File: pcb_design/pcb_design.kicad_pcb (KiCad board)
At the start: 2 copper layers, 6 parts, among them U1 ATmega2560-16AU

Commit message: Make PCB design
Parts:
- added C3: 100nF, Capacitor_SMD:C_0201_0603Metric, F.Cu at (137.2, 76.2)
- added C4: 100nF, Capacitor_SMD:C_0201_0603Metric, F.Cu at (137.2, 74.9)
- added C5: 100nF, Capacitor_SMD:C_0201_0603Metric, F.Cu at (137.2, 73.7)
- added D1: LED, LED_SMD:LED_0201_0603Metric, F.Cu at (132.1, 54.6)
- added D2: LED_PWR, LED_SMD:LED_0201_0603Metric, F.Cu at (99.1, 105.4)
- added J1: PWR_IN, Connector_PinHeader_2.54mm:PinHeader_1x02_P2.54mm_Vertical, F.Cu at (101.6, 102.9)
- added J10: PD, Connector_PinHeader_2.54mm:PinHeader_1x08_P2.54mm_Vertical, F.Cu at (171.4, 104.1)
- added J11: PE, Connector_PinHeader_2.54mm:PinHeader_1x08_P2.54mm_Vertical, F.Cu at (110.5, 43.2)
- added J12: PF, Connector_PinHeader_2.54mm:PinHeader_1x08_P2.54mm_Vertical, F.Cu at (110.5, 39.4)
- added J13: ICSP, Connector_PinHeader_2.54mm:PinHeader_2x03_P2.54mm_Vertical, F.Cu at (100.3, 88.9)
- added J14: PWR_OUT, Connector_PinHeader_2.54mm:PinHeader_1x02_P2.54mm_Vertical, F.Cu at (99.1, 99.1)
- added J2: ESP8266_CONN, Connector_PinHeader_2.54mm:PinHeader_2x04_P2.54mm_Vertical, F.Cu at (99.1, 62.2)
- added J3: PL, Connector_PinHeader_2.54mm:PinHeader_1x08_P2.54mm_Vertical, F.Cu at (149.9, 104.1)
- added J4: PK, Connector_PinHeader_2.54mm:PinHeader_1x08_P2.54mm_Vertical, F.Cu at (132.1, 39.4)
- added J5: PJ, Connector_PinHeader_2.54mm:PinHeader_1x08_P2.54mm_Vertical, F.Cu at (171.4, 61.0)
- added J6: PH, Connector_PinHeader_2.54mm:PinHeader_1x05_P2.54mm_Vertical, F.Cu at (110.5, 64.8)
- added J7: PA, Connector_PinHeader_2.54mm:PinHeader_1x08_P2.54mm_Vertical, F.Cu at (153.7, 39.4)
- added J8: PB, Connector_PinHeader_2.54mm:PinHeader_1x08_P2.54mm_Vertical, F.Cu at (110.5, 81.3)
- added J9: PC, Connector_PinHeader_2.54mm:PinHeader_1x08_P2.54mm_Vertical, F.Cu at (171.4, 82.5)
- added R3: 10K, Resistor_SMD:R_0201_0603Metric, F.Cu at (100.3, 59.7)
- added R4: 20K, Resistor_SMD:R_0201_0603Metric, F.Cu at (97.8, 59.7)
- added R7: 1K, Resistor_SMD:R_0201_0603Metric, F.Cu at (130.8, 54.6)
- added R8: 10K, Resistor_SMD:R_0201_0603Metric, F.Cu at (102.9, 86.4)
- added R9: 1K, Resistor_SMD:R_0201_0603Metric, F.Cu at (100.3, 105.4)
- added SW1: SW_Push, Button_Switch_SMD:SW_SPST_B3U-1000P, F.Cu at (99.1, 83.8)
- added U2: LD1117S33TR_SOT223, Package_TO_SOT_SMD:SOT-223-3_TabPin2, F.Cu at (101.6, 76.2)
- C1, C2: footprint Capacitor_SMD:C_0603_1608Metric -> Capacitor_SMD:C_0201_0603Metric
- R1, R2: footprint Resistor_SMD:R_1806_4516Metric_Pad1.57x1.80mm_HandSolder -> Resistor_SMD:R_0201_0603Metric
- moved R1 52.8 mm to (139.7, 88.9), turned to 180 degrees
- moved C2 39.9 mm to (138.4, 86.4), turned to 90 degrees
- moved Clk1 36.0 mm to (142.2, 82.5), turned to 180 degrees
- moved C1 35.3 mm to (141.0, 86.4), turned to 90 degrees
- moved R2 27.4 mm to (138.4, 77.5), turned to 270 degrees
- moved U1 12.8 mm to (141.0, 63.5)
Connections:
- net /GND renamed GND
- net Net-(U1-Pad51) renamed /PG0
- net Net-(U1-Pad52) renamed /PG1
- U1 pad 10: Net-(U1-Pad10) -> +5V
- U1 pad 100: Net-(U1-Pad100) -> +5V
- U1 pad 12: Net-(U1-Pad12) -> /ESP_TX
- U1 pad 13: Net-(U1-Pad13) -> /TX2
- U1 pad 2: Net-(U1-Pad2) -> /PRGM_RX
- U1 pad 20: Net-(U1-Pad20) -> /SCK
- U1 pad 21: Net-(U1-Pad21) -> /MOSI
- U1 pad 22: Net-(U1-Pad22) -> /MISO
- U1 pad 3: Net-(U1-Pad3) -> /PRGM_TX
- U1 pad 31: Net-(U1-Pad10) -> +5V
- U1 pad 61: Net-(U1-Pad10) -> +5V
- U1 pad 80: Net-(U1-Pad10) -> +5V
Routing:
- net +5V: track 0.00 -> 136.8 mm
- net /RST: track 0.00 -> 72.1 mm
- net /ESP_TX: track 0.00 -> 53.9 mm
- net /MISO: track 0.00 -> 48.2 mm
- net Net-(J10-Pad1): track 0.00 -> 44.6 mm
- net Net-(J5-Pad8): track 0.00 -> 43.3 mm
- net /SCK: track 0.00 -> 43.3 mm
- net Net-(J3-Pad8): track 0.00 -> 43.2 mm
- net Net-(J3-Pad7): track 0.00 -> 42.4 mm
- net Net-(J10-Pad2): track 0.00 -> 41.8 mm
- net Net-(J3-Pad6): track 0.00 -> 41.5 mm
- net Net-(J3-Pad5): track 0.00 -> 40.7 mm
- net /MOSI: track 0.00 -> 40.4 mm
- net Net-(J10-Pad3): track 0.00 -> 40.1 mm
- net Net-(J3-Pad4): track 0.00 -> 39.9 mm
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- added copper zone on B.Cu, net GND

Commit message: Almost done?
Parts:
- added JP1: IO0_JMP, Connector_PinHeader_2.54mm:PinHeader_1x02_P2.54mm_Vertical, F.Cu at (99.1, 45.7)
- added JP2: RST_JMP, Connector_PinHeader_2.54mm:PinHeader_1x02_P2.54mm_Vertical, F.Cu at (102.9, 45.7)
- added R5: 10k, Resistor_SMD:R_0201_0603Metric, F.Cu at (100.3, 52.1)
- added R6: 10k, Resistor_SMD:R_0201_0603Metric, F.Cu at (101.6, 52.1)
- D1: value LED -> FUN_LED_YEL
- D2: value LED_PWR -> LED_PWR_GRN
- moved R3 4.02 mm to (99.1, 55.9)
- moved J14 3.81 mm to (102.9, 99.1), turned to 270 degrees
- moved J2 3.81 mm to (99.1, 58.4)
- moved R4 3.81 mm to (97.8, 55.9)
- moved R8 1.59 mm to (101.3, 86.4), turned to 180 degrees
- moved J1 1.27 mm to (102.9, 102.9)
- moved R7 1.27 mm to (132.1, 54.6)
- moved D2 1.27 mm to (100.3, 105.4)
- moved J13 1.27 mm to (99.1, 88.9)
- moved R9 1.27 mm to (101.6, 105.4)
- moved U2 1.27 mm to (101.6, 74.9)
- moved D1 1.27 mm to (133.3, 54.6)
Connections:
- J14 pad 1: GND -> +5V
- J14 pad 2: +5V -> GND
- J2 pad 3: +3V3 -> /ESP_IO0
- J2 pad 4: +3V3 -> /ESP_RST
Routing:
- net GND: track 52.9 -> 186.2 mm, vias 9 -> 11
- net /ESP_IO0: track 0.00 -> 22.7 mm
- net /ESP_TX: track 53.9 -> 33.0 mm
- net /ESP_RST: track 0.00 -> 18.8 mm
- net Net-(J5-Pad8): track 43.3 -> 33.7 mm, vias 0 -> 2
- net /TX2: track 34.1 -> 42.2 mm, vias 0 -> 2
- net +3V3: track 24.3 -> 31.7 mm, vias 0 -> 2
- net +5V: track 136.8 -> 139.9 mm
- net /MISO: track 48.2 -> 50.1 mm
- net /MOSI: track 40.4 -> 41.6 mm
- net /SCK: track 43.3 -> 44.5 mm
- net /ESP_RX: track 4.44 -> 3.30 mm
- net /RST: track 72.1 -> 73.2 mm, vias 0 -> 1
- net Net-(D2-Pad2): track 0.00 -> 0.63 mm
- removed copper zone on B.Cu, net GND
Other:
- board text added: "3.3V"
- board text added: "5V"
- board text added: "A0"
- board text added: "B0"
- board text added: "C0"
- board text added: "D7"
- board text added: "E0"
- board text added: "ESP"
- board text added: "ESP JMP"
- board text added: "F0"
- board text added: "GND"
- board text added: "H2"
- board text added: "ICSP"
- board text added: "IO0"
- board text added: "J0"
- board text added: "K0"
- board text added: "L0"
- board text added: "RST"

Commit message: Add DS3231 RTC header
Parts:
- added J15: Conn_01x04, Connector_PinSocket_2.54mm:PinSocket_1x04_P2.54mm_Vertical, F.Cu at (134.6, 100.3)
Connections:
- net Net-(J10-Pad1) renamed /SCL
- net Net-(J10-Pad2) renamed /SDA
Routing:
- net /SDA: track 41.8 -> 82.3 mm
- net /SCL: track 44.6 -> 85.1 mm
- net +5V: track 139.9 -> 153.4 mm
- net GND: track 186.2 -> 193.6 mm

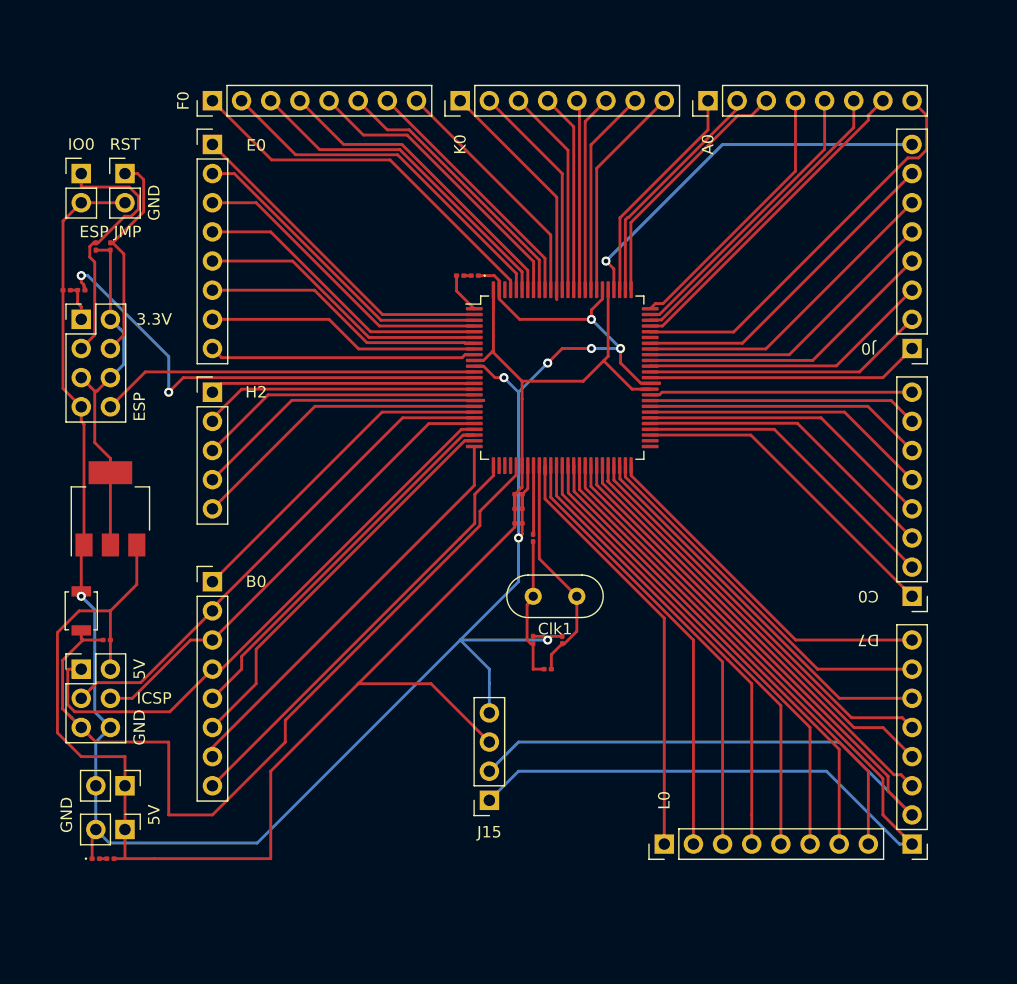
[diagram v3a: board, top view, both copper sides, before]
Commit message: Add lineout to PCB design
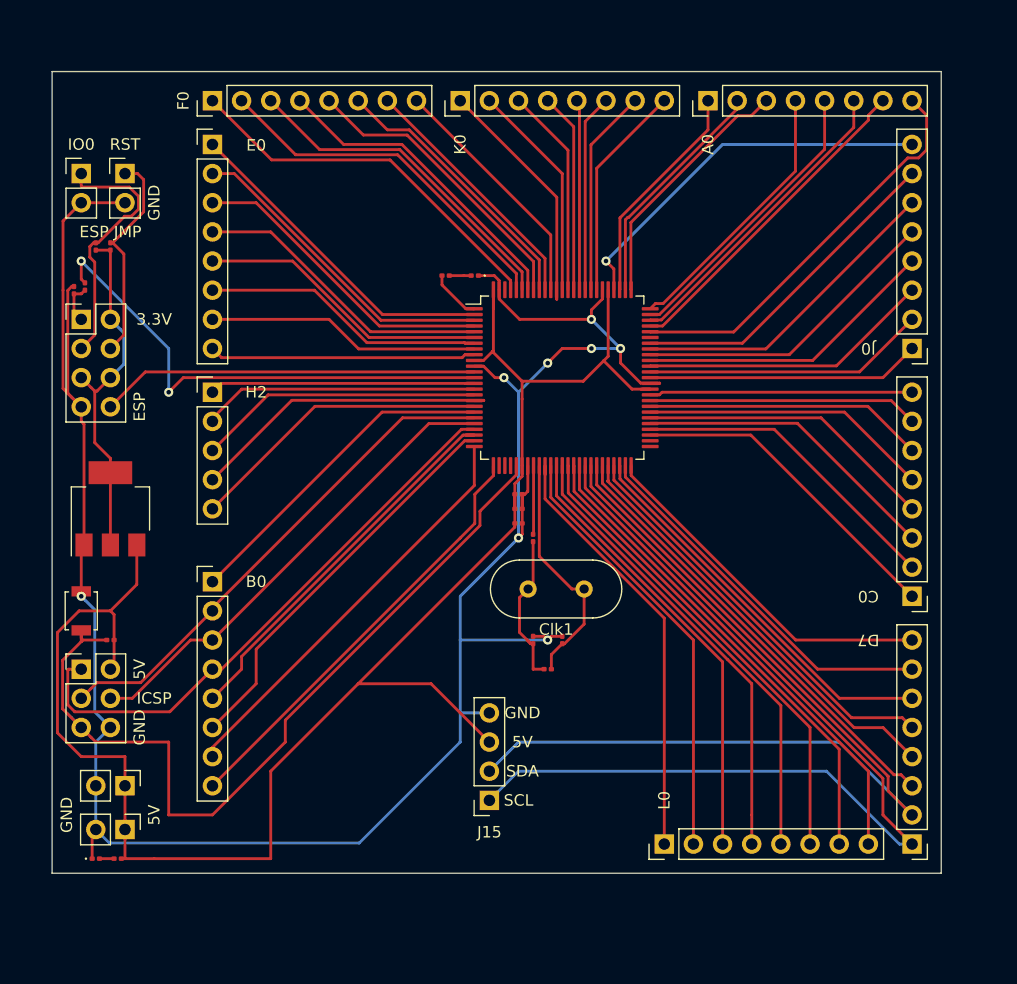
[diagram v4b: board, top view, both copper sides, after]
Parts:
- Clk1: footprint Crystal:Crystal_HC52-8mm_Vertical -> Crystal:Crystal_HC49-4H_Vertical
- moved R7 1.27 mm to (130.8, 54.6)
- moved Clk1 0.90 mm to (142.9, 81.9)
- moved R9 0.64 mm to (102.2, 105.4)
- moved R4 0.63 mm to (98.4, 55.9), turned to 90 degrees
- moved R3 0.45 mm to (99.4, 55.6), turned to 270 degrees
- moved R8 0.32 mm to (101.6, 86.4)
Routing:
- net GND: track 193.6 -> 205.4 mm
- net /TX2: track 42.2 -> 43.8 mm
- net Net-(C1-Pad1): track 20.1 -> 21.5 mm
- net Net-(D1-Pad2): track 0.63 -> 1.90 mm
- net /RST: track 73.2 -> 74.3 mm
- net Net-(C2-Pad1): track 12.6 -> 13.6 mm
- net Net-(R7-Pad2): track 3.86 -> 4.62 mm
- net Net-(D2-Pad2): track 0.63 -> 1.27 mm
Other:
- board outline added: 77.5 x 69.9 mm
- board text added: "SCL"
- board text added: "SDA"

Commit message: Add mounting holes
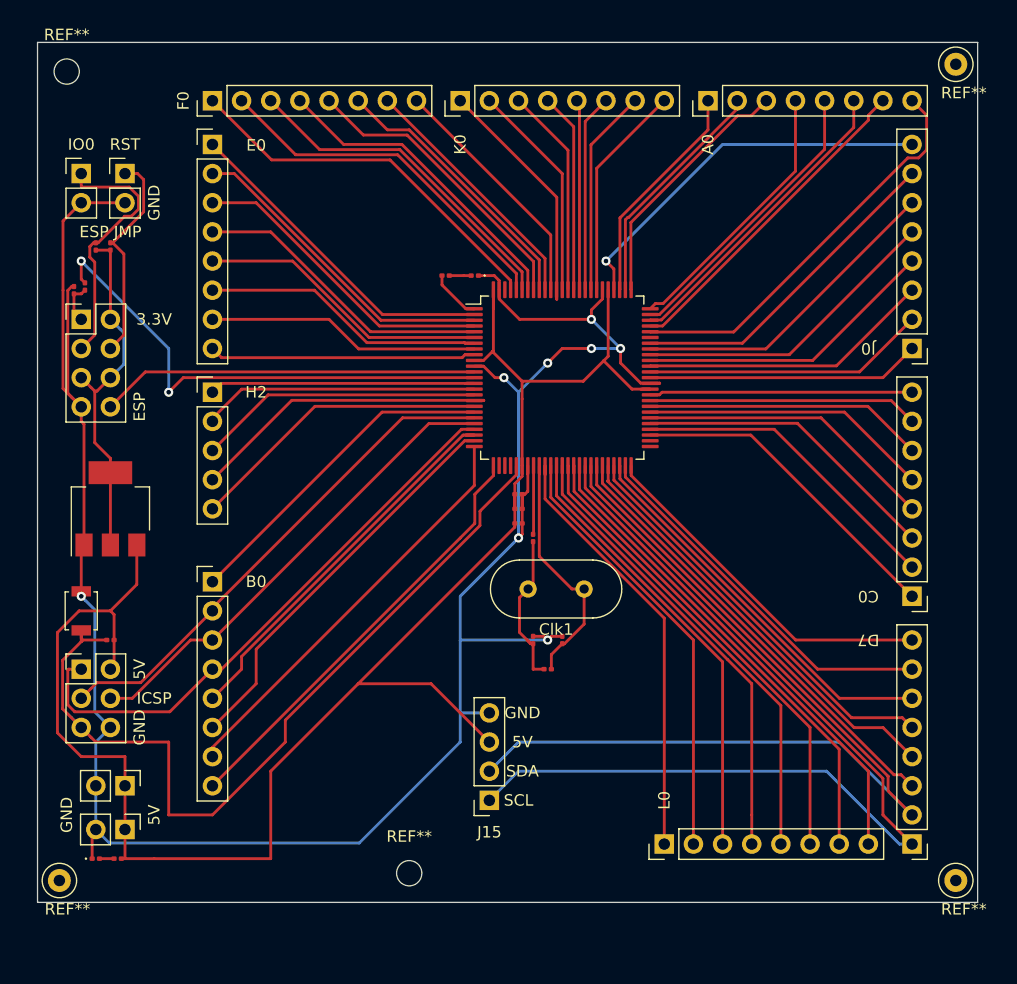
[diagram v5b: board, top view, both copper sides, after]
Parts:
- added REF**: TestPoint_Loop_D1.80mm_Drill1.0mm_Beaded, TestPoint:TestPoint_Loop_D1.80mm_Drill1.0mm_Beaded, F.Cu at (97.2, 107.3)
- added REF**: TestPoint_Loop_D1.80mm_Drill1.0mm_Beaded, TestPoint:TestPoint_Loop_D1.80mm_Drill1.0mm_Beaded, F.Cu at (175.3, 107.3)
- added REF**: TestPoint_Loop_D1.80mm_Drill1.0mm_Beaded, TestPoint:TestPoint_Loop_D1.80mm_Drill1.0mm_Beaded, F.Cu at (175.3, 36.2)
- added REF**: MountingHole_2.2mm_M2, MountingHole:MountingHole_2.2mm_M2, F.Cu at (127.6, 106.7)
- added REF**: MountingHole_2.2mm_M2, MountingHole:MountingHole_2.2mm_M2, F.Cu at (97.8, 36.8)
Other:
- board size 77.5 x 69.9 mm -> 81.9 x 74.9 mm
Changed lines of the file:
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@@
     (tracks 513)
     (zones 0)
-    (modules 37)
+    (modules 42)
     (nets 100)
   )
@@
     (add_net "Net-(U1-Pad98)")
   )
+  (module TestPoint:TestPoint_Loop_D1.80mm_Drill1.0mm_Beaded (layer F.Cu)
+    (at 97.155 107.315)
+    (descr "wire loop with bead as test point, loop diameter 1.8mm, hole diameter 1.0mm")
+    (tags "test point wire loop bead")
+    (fp_text reference REF** (at 0.7 2.5) (layer F.SilkS)
+      (effects (font (size 1 1) (thickness 0.15)))
+    )
+    (fp_text value TestPoint_Loop_D1.80mm_Drill1.0mm_Beaded (at 0 -2.8) (layer F.Fab)
+      (effects (font (size 1 1) (thickness 0.15)))
+    )
+    (fp_text user %R (at 0.7 2.5) (layer F.Fab)
+      (effects (font (size 1 1) (thickness 0.15)))
+    )
+    (fp_circle (center 0 0) (end 1.3 0) (layer F.Fab) (width 0.12))
+    (fp_line (start -0.9 0.2) (end -0.9 -0.2) (layer F.Fab) (width 0.12))
+    (fp_line (start 0.9 0.2) (end -0.9 0.2) (layer F.Fab) (width 0.12))
+    (fp_line (start 0.9 -0.2) (end 0.9 0.2) (layer F.Fab) (width 0.12))
+    (fp_line (start -0.9 -0.2) (end 0.9 -0.2) (layer F.Fab) (width 0.12))
+    (fp_circle (center 0 0) (end 1.5 0) (layer F.SilkS) (width 0.12))
+    (fp_circle (center 0 0) (end 1.8 0) (layer F.CrtYd) (width 0.05))
+    (pad 1 thru_hole circle (at 0 0) (size 2 2) (drill 1) (layers *.Cu *.Mask))
+    (model ${KISYS3DMOD}/TestPoint.3dshapes/TestPoint_Loop_D1.80mm_Drill1.0mm_Beaded.wrl
+      (at (xyz 0 0 0))
+      (scale (xyz 1 1 1))
+      (rotate (xyz 0 0 0))
+    )
+  )
+  (module TestPoint:TestPoint_Loop_D1.80mm_Drill1.0mm_Beaded (layer F.Cu)
+    (at 175.26 107.315)
+    (descr "wire loop with bead as test point, loop diameter 1.8mm, hole diameter 1.0mm")
+    (tags "test point wire loop bead")
+    (fp_text reference REF** (at 0.7 2.5) (layer F.SilkS)
+      (effects (font (size 1 1) (thickness 0.15)))
+    )
+    (fp_text value TestPoint_Loop_D1.80mm_Drill1.0mm_Beaded (at 0 -2.8) (layer F.Fab)
+      (effects (font (size 1 1) (thickness 0.15)))
+    )
+    (fp_text user %R (at 0.7 2.5) (layer F.Fab)
+      (effects (font (size 1 1) (thickness 0.15)))
+    )
+    (fp_circle (center 0 0) (end 1.3 0) (layer F.Fab) (width 0.12))
+    (fp_line (start -0.9 0.2) (end -0.9 -0.2) (layer F.Fab) (width 0.12))
+    (fp_line (start 0.9 0.2) (end -0.9 0.2) (layer F.Fab) (width 0.12))
+    (fp_line (start 0.9 -0.2) (end 0.9 0.2) (layer F.Fab) (width 0.12))
+    (fp_line (start -0.9 -0.2) (end 0.9 -0.2) (layer F.Fab) (width 0.12))
+    (fp_circle (center 0 0) (end 1.5 0) (layer F.SilkS) (width 0.12))
+    (fp_circle (center 0 0) (end 1.8 0) (layer F.CrtYd) (width 0.05))
+    (pad 1 thru_hole circle (at 0 0) (size 2 2) (drill 1) (layers *.Cu *.Mask))
+    (model ${KISYS3DMOD}/TestPoint.3dshapes/TestPoint_Loop_D1.80mm_Drill1.0mm_Beaded.wrl
+      (at (xyz 0 0 0))
+      (scale (xyz 1 1 1))
+      (rotate (xyz 0 0 0))
+    )
+  )
+  (module TestPoint:TestPoint_Loop_D1.80mm_Drill1.0mm_Beaded (layer F.Cu)
+    (at 175.26 36.195)
+    (descr "wire loop with bead as test point, loop diameter 1.8mm, hole diameter 1.0mm")
+    (tags "test point wire loop bead")
+    (fp_text reference REF** (at 0.7 2.5) (layer F.SilkS)
+      (effects (font (size 1 1) (thickness 0.15)))
+    )
+    (fp_text value TestPoint_Loop_D1.80mm_Drill1.0mm_Beaded (at 0 -2.8) (layer F.Fab)
+      (effects (font (size 1 1) (thickness 0.15)))
+    )
+    (fp_text user %R (at 0.7 2.5) (layer F.Fab)
+      (effects (font (size 1 1) (thickness 0.15)))
+    )
+    (fp_circle (center 0 0) (end 1.3 0) (layer F.Fab) (width 0.12))
+    (fp_line (start -0.9 0.2) (end -0.9 -0.2) (layer F.Fab) (width 0.12))
+    (fp_line (start 0.9 0.2) (end -0.9 0.2) (layer F.Fab) (width 0.12))
+    (fp_line (start 0.9 -0.2) (end 0.9 0.2) (layer F.Fab) (width 0.12))
+    (fp_line (start -0.9 -0.2) (end 0.9 -0.2) (layer F.Fab) (width 0.12))
+    (fp_circle (center 0 0) (end 1.5 0) (layer F.SilkS) (width 0.12))
+    (fp_circle (center 0 0) (end 1.8 0) (layer F.CrtYd) (width 0.05))
+    (pad 1 thru_hole circle (at 0 0) (size 2 2) (drill 1) (layers *.Cu *.Mask))
+    (model ${KISYS3DMOD}/TestPoint.3dshapes/TestPoint_Loop_D1.80mm_Drill1.0mm_Beaded.wrl
+      (at (xyz 0 0 0))
+      (scale (xyz 1 1 1))
+      (rotate (xyz 0 0 0))
+    )
+  )
+  (module MountingHole:MountingHole_2.2mm_M2 (layer F.Cu)
+    (at 127.635 106.68)
+    (descr "Mounting Hole 2.2mm, no annular, M2")
+    (tags "mounting hole 2.2mm no annular m2")
+    (attr virtual)
+    (fp_text reference REF** (at 0 -3.2) (layer F.SilkS)
+      (effects (font (size 1 1) (thickness 0.15)))
+    )
+    (fp_text value MountingHole_2.2mm_M2 (at 0 3.2) (layer F.Fab)
+      (effects (font (size 1 1) (thickness 0.15)))
+    )
+    (fp_circle (center 0 0) (end 2.45 0) (layer F.CrtYd) (width 0.05))
+    (fp_circle (center 0 0) (end 2.2 0) (layer Cmts.User) (width 0.15))
+    (fp_text user %R (at 0.3 0) (layer F.Fab)
+      (effects (font (size 1 1) (thickness 0.15)))
+    )
+    (pad 1 np_thru_hole circle (at 0 0) (size 2.2 2.2) (drill 2.2) (layers *.Cu *.Mask))
+  )
+  (module MountingHole:MountingHole_2.2mm_M2 (layer F.Cu)
+    (at 97.79 36.83)
+    (descr "Mounting Hole 2.2mm, no annular, M2")
+    (tags "mounting hole 2.2mm no annular m2")
+    (attr virtual)
+    (fp_text reference REF** (at 0 -3.2) (layer F.SilkS)
+      (effects (font (size 1 1) (thickness 0.15)))
+    )
+    (fp_text value MountingHole_2.2mm_M2 (at 0 3.2) (layer F.Fab)
+      (effects (font (size 1 1) (thickness 0.15)))
+    )
+    (fp_circle (center 0 0) (end 2.45 0) (layer F.CrtYd) (width 0.05))
+    (fp_circle (center 0 0) (end 2.2 0) (layer Cmts.User) (width 0.15))
+    (fp_text user %R (at 0.3 0) (layer F.Fab)
+      (effects (font (size 1 1) (thickness 0.15)))
+    )
+    (pad 1 np_thru_hole circle (at 0 0) (size 2.2 2.2) (drill 2.2) (layers *.Cu *.Mask))
+  )
   (module Crystal:Crystal_HC49-4H_Vertical (layer F.Cu)
     (at 142.875 81.915 180)
@@
     )
   )
-  (gr_line (start 173.99 36.83) (end 173.99 106.68) (layer Edge.Cuts) (width 0.1))
-  (gr_line (start 96.52 36.83) (end 173.99 36.83) (layer Edge.Cuts) (width 0.1))
-  (gr_line (start 96.52 106.68) (end 96.52 36.83) (layer Edge.Cuts) (width 0.1))
-  (gr_line (start 173.99 106.68) (end 96.52 106.68) (layer Edge.Cuts) (width 0.1))
+  (gr_line (start 177.165 34.29) (end 177.165 109.22) (layer Edge.Cuts) (width 0.1))
+  (gr_line (start 95.25 34.29) (end 177.165 34.29) (layer Edge.Cuts) (width 0.1))
+  (gr_line (start 95.25 109.22) (end 95.25 34.29) (layer Edge.Cuts) (width 0.1))
+  (gr_line (start 177.165 109.22) (end 95.25 109.22) (layer Edge.Cuts) (width 0.1))
   (gr_text GND (at 137.5 92.71) (layer F.SilkS)
     (effects (font (size 1 1) (thickness 0.15)))
